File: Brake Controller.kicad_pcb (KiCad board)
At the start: 2 copper layers, 35.6 x 38.1 mm, 28 parts, among them J1 INPUT, J2 OUTPUT, Q1 Q_PMOS_GDS, U1 IFX007T, U2 IFX007T

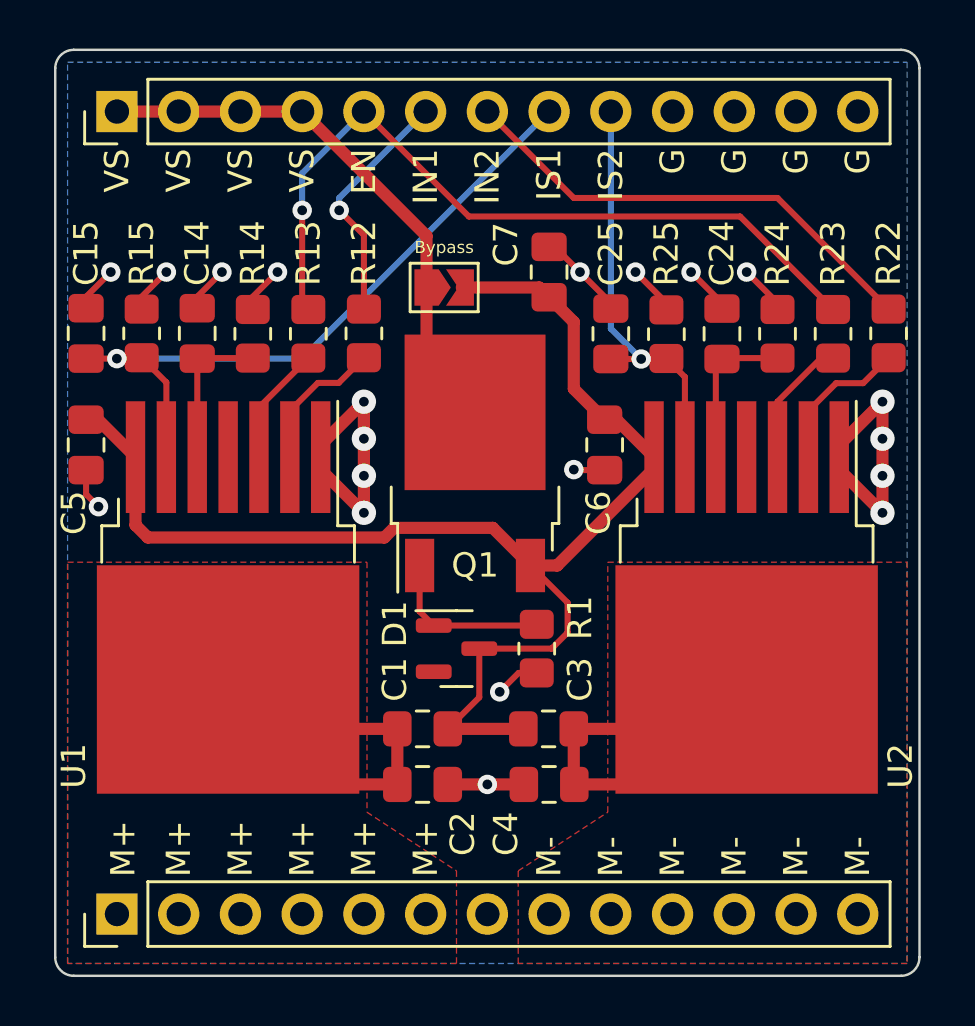
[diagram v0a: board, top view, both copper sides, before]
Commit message: Add larger ground pour to motor driver pin 1
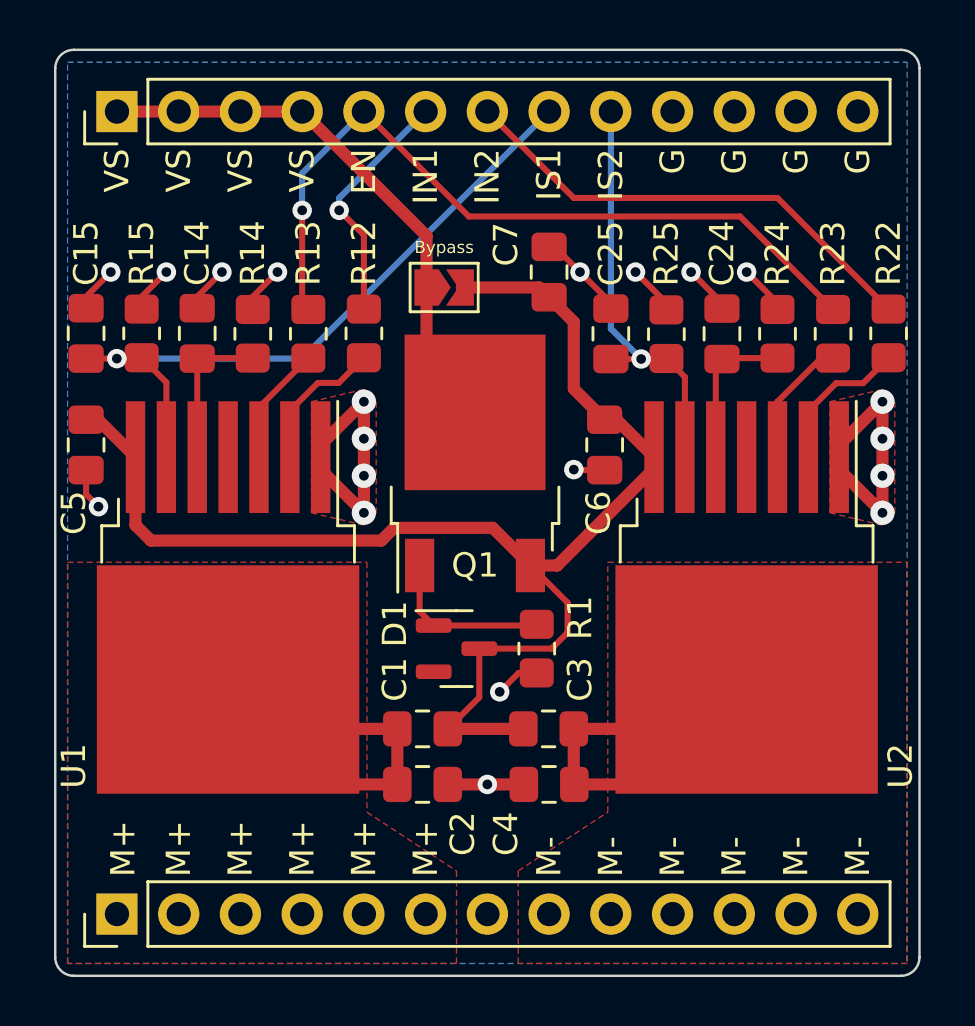
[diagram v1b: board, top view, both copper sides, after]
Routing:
- added copper zone on F.Cu, net GND
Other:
- board text added: "Autonomous Motorsports Purdue Brake Controller Breakout Revision A 2022-04-11"
- board text removed: "Autonomous Motorsports Purdue Brake Controller Breakout Revision A 2022-04-09"
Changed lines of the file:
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@@
   (gr_arc (start 122.682 124.46) (mid 122.143185 124.236815) (end 121.92 123.698) (layer "Edge.Cuts") (width 0.1))
   (gr_line (start 122.682 124.46) (end 156.718 124.46) (layer "Edge.Cuts") (width 0.1))
-  (gr_text "Autonomous Motorsports Purdue\nBrake Controller Breakout\nRevision A\n2022-04-09" (at 154.94 93.98) (layer "B.SilkS")
+  (gr_text "Autonomous Motorsports Purdue\nBrake Controller Breakout\nRevision A\n2022-04-11" (at 154.94 93.98) (layer "B.SilkS")
     (effects (font (size 1 1) (thickness 0.15)) (justify left mirror))
   )
@@
   )
   (segment (start 123.19 101.5785) (end 123.6825 101.5785) (width 0.5) (layer "F.Cu") (net 1))
-  (segment (start 125.73 106.426) (end 135.465978 106.426) (width 0.5) (layer "F.Cu") (net 1))
   (segment (start 138.0705 114.3) (end 141.181 114.3) (width 0.5) (layer "F.Cu") (net 1))
   (segment (start 144.526 101.5785) (end 145.0185 101.5785) (width 0.5) (layer "F.Cu") (net 1))
-  (segment (start 135.465978 106.426) (end 135.863489 106.028489) (width 0.5) (layer "F.Cu") (net 1))
+  (segment (start 125.222 105.918) (end 125.857 106.553) (width 0.5) (layer "F.Cu") (net 1))
+  (segment (start 135.863489 106.028489) (end 139.923489 106.028489) (width 0.5) (layer "F.Cu") (net 1))
   (segment (start 123.6825 101.5785) (end 125.222 103.118) (width 0.5) (layer "F.Cu") (net 1))
   (segment (start 146.558 103.593) (end 146.558 103.118) (width 0.5) (layer "F.Cu") (net 1))
@@
   (segment (start 142.344493 110.998) (end 143.002 110.340493) (width 0.25) (layer "F.Cu") (net 1))
   (segment (start 144.526 101.5785) (end 143.256 100.3085) (width 0.5) (layer "F.Cu") (net 1))
+  (segment (start 125.222 103.118) (end 125.222 105.918) (width 0.5) (layer "F.Cu") (net 1))
   (segment (start 143.256 97.5575) (end 142.24 96.5415) (width 0.5) (layer "F.Cu") (net 1))
   (segment (start 139.3675 113.003) (end 138.0705 114.3) (width 0.25) (layer "F.Cu") (net 1))
-  (segment (start 125.222 105.918) (end 125.73 106.426) (width 0.5) (layer "F.Cu") (net 1))
+  (segment (start 141.8375 96.139) (end 142.24 96.5415) (width 0.5) (layer "F.Cu") (net 1))
+  (segment (start 125.857 106.553) (end 135.338978 106.553) (width 0.5) (layer "F.Cu") (net 1))
+  (segment (start 141.473 107.578) (end 142.573 107.578) (width 0.5) (layer "F.Cu") (net 1))
   (segment (start 139.923489 106.028489) (end 141.473 107.578) (width 0.5) (layer "F.Cu") (net 1))
-  (segment (start 141.8375 96.139) (end 142.24 96.5415) (width 0.5) (layer "F.Cu") (net 1))
-  (segment (start 135.863489 106.028489) (end 139.923489 106.028489) (width 0.5) (layer "F.Cu") (net 1))
-  (segment (start 141.473 107.578) (end 142.573 107.578) (width 0.5) (layer "F.Cu") (net 1))
   (segment (start 142.573 107.578) (end 146.558 103.593) (width 0.5) (layer "F.Cu") (net 1))
   (segment (start 145.0185 101.5785) (end 146.558 103.118) (width 0.5) (layer "F.Cu") (net 1))
   (segment (start 138.647 96.139) (end 141.8375 96.139) (width 0.5) (layer "F.Cu") (net 1))
+  (segment (start 135.338978 106.553) (end 135.863489 106.028489) (width 0.5) (layer "F.Cu") (net 1))
   (segment (start 143.256 100.3085) (end 143.256 97.5575) (width 0.5) (layer "F.Cu") (net 1))
   (segment (start 143.002 109.107) (end 141.473 107.578) (width 0.25) (layer "F.Cu") (net 1))
   (segment (start 139.3675 110.998) (end 139.3675 113.003) (width 0.25) (layer "F.Cu") (net 1))
   (segment (start 143.002 110.340493) (end 143.002 109.107) (width 0.25) (layer "F.Cu") (net 1))
-  (segment (start 125.222 103.118) (end 125.222 105.918) (width 0.5) (layer "F.Cu") (net 1))
   (segment (start 125.476 96.52) (end 126.492 95.504) (width 0.25) (layer "F.Cu") (net 2))
   (segment (start 144.78 97.0065) (end 144.78 96.774) (width 0.25) (layer "F.Cu") (net 2))
@@
     )
   )
+  (zone (net 2) (net_name "GND") (layer "F.Cu") (hatch edge 0.508)
+    (connect_pads yes (clearance 0.508))
+    (min_thickness 0.254) (filled_areas_thickness no)
+    (fill yes (thermal_gap 0.508) (thermal_bridge_width 0.508))
+    (polygon
+      (pts
+        (xy 156.464 100.838)
+        (xy 156.464 105.41)
+        (xy 155.956 105.918)
+        (xy 153.797 105.41)
+        (xy 153.797 100.838)
+        (xy 155.956 100.33)
+      )
+    )
+  )
   (zone (net 19) (net_name "/MOTOR-") (layer "F.Cu") (hatch edge 0.508)
     (connect_pads yes (clearance 0.508))
@@
       )
     )
+  )
+  (zone (net 2) (net_name "GND") (layer "F.Cu") (hatch edge 0.508)
+    (connect_pads yes (clearance 0.508))
+    (min_thickness 0.254) (filled_areas_thickness no)
+    (fill yes (thermal_gap 0.508) (thermal_bridge_width 0.508))
+    (polygon
+      (pts
+        (xy 135.128 100.838)
+        (xy 135.128 105.41)
+        (xy 134.62 105.918)
+        (xy 132.461 105.41)
+        (xy 132.461 100.838)
+        (xy 134.62 100.33)
+      )
+    )

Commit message: Add thermal relief to motor controller connections
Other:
- board text added: "Autonomous Motorsports Purdue Brake Controller Breakout Revision B 2022-04-22"
- board text removed: "Autonomous Motorsports Purdue Brake Controller Breakout Revision A 2022-04-11"
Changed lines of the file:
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@@
   (gr_arc (start 122.682 124.46) (mid 122.143185 124.236815) (end 121.92 123.698) (layer "Edge.Cuts") (width 0.1))
   (gr_line (start 122.682 124.46) (end 156.718 124.46) (layer "Edge.Cuts") (width 0.1))
-  (gr_text "Autonomous Motorsports Purdue\nBrake Controller Breakout\nRevision A\n2022-04-11" (at 154.94 93.98) (layer "B.SilkS")
+  (gr_text "Autonomous Motorsports Purdue\nBrake Controller Breakout\nRevision B\n2022-04-22" (at 154.94 93.98) (layer "B.SilkS")
     (effects (font (size 1 1) (thickness 0.15)) (justify left mirror))
   )
@@
   (segment (start 143.256 114.3) (end 143.256 116.5645) (width 0.5) (layer "F.Cu") (net 19))
   (zone (net 18) (net_name "/MOTOR+") (layer "F.Cu") (hatch edge 0.508)
-    (connect_pads yes (clearance 0.508))
+    (connect_pads (clearance 0.508))
     (min_thickness 0.254) (filled_areas_thickness no)
     (fill yes (thermal_gap 0.508) (thermal_bridge_width 0.508))
@@
   )
   (zone (net 19) (net_name "/MOTOR-") (layer "F.Cu") (hatch edge 0.508)
-    (connect_pads yes (clearance 0.508))
+    (connect_pads (clearance 0.508))
     (min_thickness 0.254) (filled_areas_thickness no)
     (fill yes (thermal_gap 0.508) (thermal_bridge_width 0.508))
